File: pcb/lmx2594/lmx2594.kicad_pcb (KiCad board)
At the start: 4 copper layers, 48.3 x 48.3 mm, 87 parts, among them J1 Conn_Coaxial, J2 Conn_Coaxial, J3 Conn_01x13_Male, J4 Conn_Coaxial, J5 Conn_Coaxial, J6 Conn_Coaxial, J7 Conn_Coaxial, J8 Conn_Coaxial, J9 Conn_Coaxial, U1 L7812, U2 TPS62150, U3 lmx254

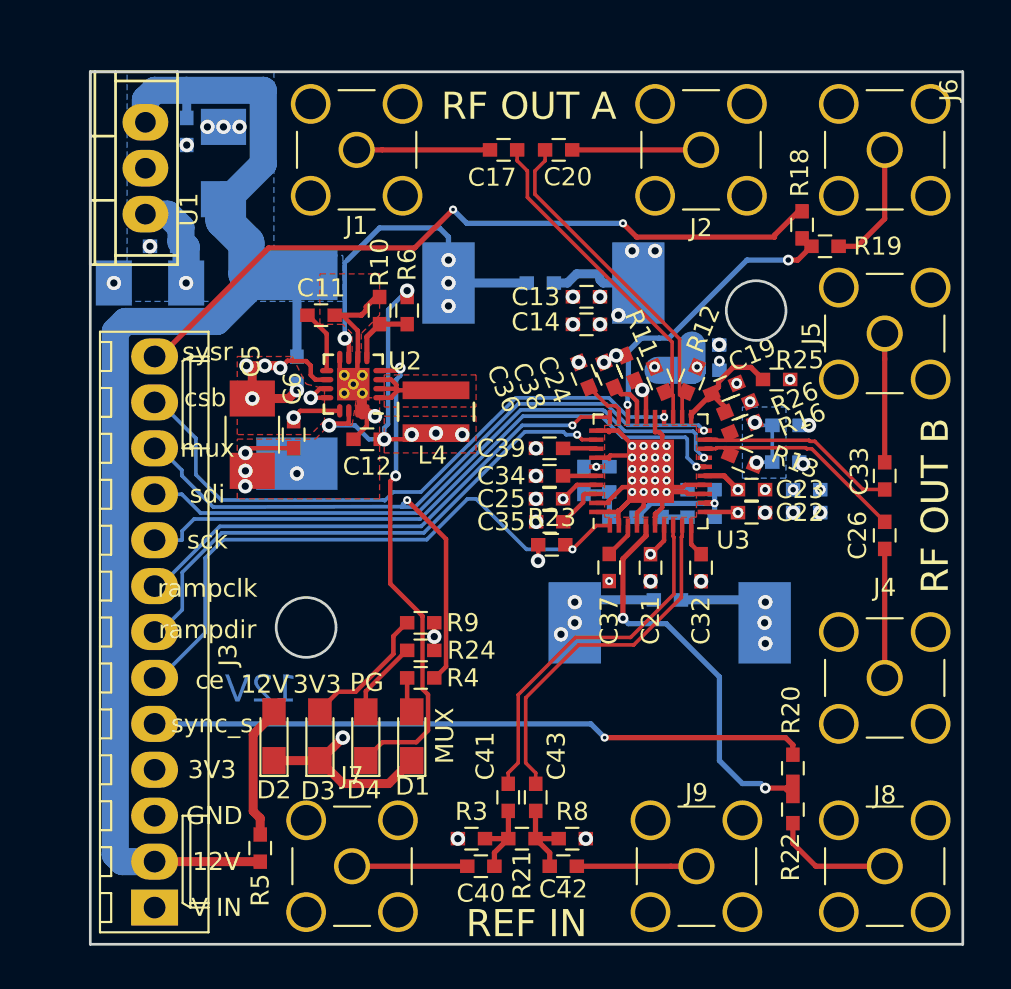
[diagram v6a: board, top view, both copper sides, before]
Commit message: additional fixes to silkscreen
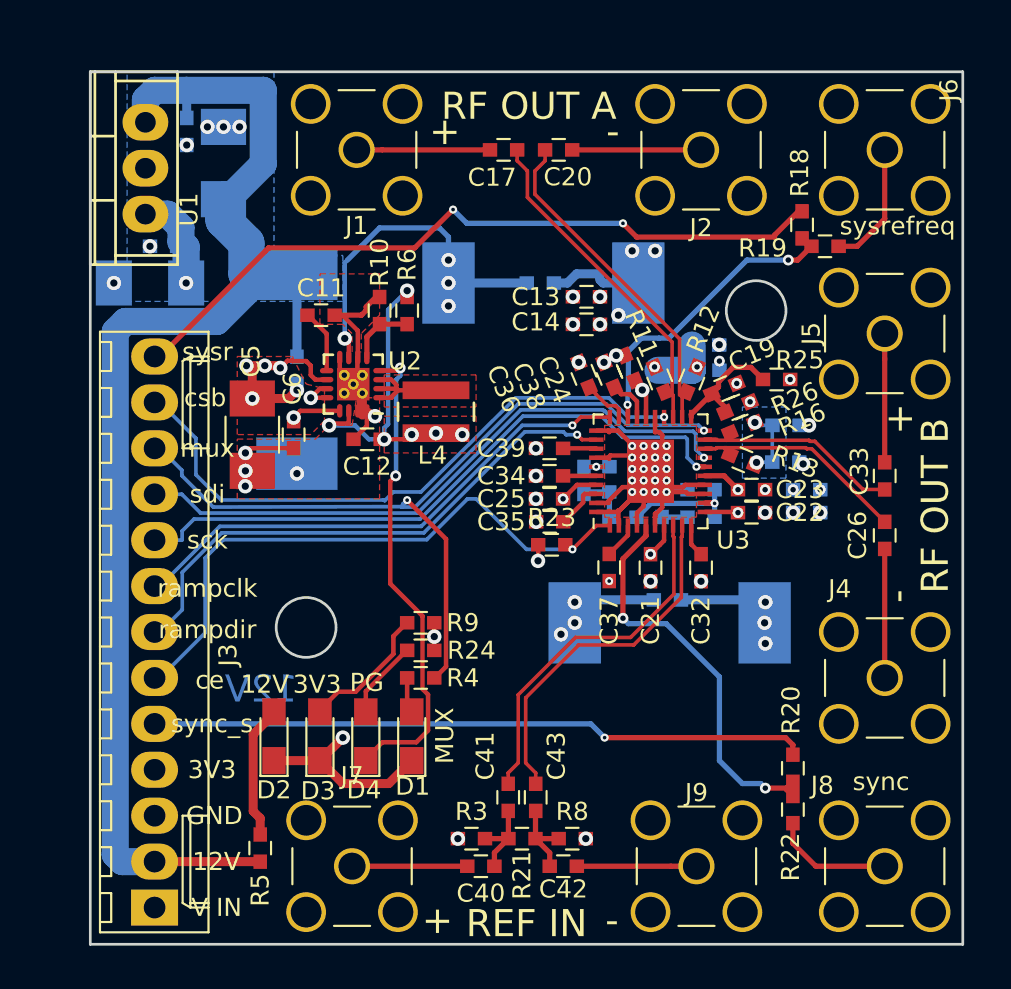
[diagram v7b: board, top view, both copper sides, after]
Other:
- board text added: "+"
- board text added: "-"
- board text added: "sync"
- board text added: "sysrefreq"
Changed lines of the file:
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@@
   (general
     (thickness 1.6)
-    (drawings 29)
+    (drawings 37)
     (tracks 902)
     (zones 0)
@@
   (page A4)
   (layers
-    (0 F.Cu signal)
+    (0 F.Cu signal hide)
     (1 In1.Cu signal hide)
     (2 In2.Cu signal hide)
@@
     (34 B.Paste user hide)
     (35 F.Paste user hide)
-    (36 B.SilkS user hide)
-    (37 F.SilkS user)
+    (36 B.SilkS user)
+    (37 F.SilkS user hide)
     (38 B.Mask user hide)
     (39 F.Mask user hide)
@@
     (descr "SMA pcb through hole jack")
     (tags "SMA THT Jack Straight")
-    (fp_text reference J4 (at 0 -5) (layer F.SilkS)
+    (fp_text reference J4 (at -2.4892 -4.9276) (layer F.SilkS)
       (effects (font (size 1 1) (thickness 0.15)))
     )
@@
     (descr "SMA pcb through hole jack")
     (tags "SMA THT Jack Straight")
-    (fp_text reference J8 (at 0 -3.937) (layer F.SilkS)
+    (fp_text reference J8 (at -3.4544 -4.4704) (layer F.SilkS)
       (effects (font (size 1 1) (thickness 0.15)))
     )
@@
     (tags "capacitor 0603")
     (attr smd)
-    (fp_text reference R19 (at 2.921 0) (layer F.SilkS)
+    (fp_text reference R19 (at -3.4544 0.1016) (layer F.SilkS)
       (effects (font (size 1 1) (thickness 0.15)))
     )
@@
     )
   )
+  (gr_text sync (at 117.3988 110.3884) (layer F.SilkS)
+    (effects (font (size 1 1) (thickness 0.25)))
+  )
+  (gr_text sysrefreq (at 118.3132 79.6544) (layer F.SilkS)
+    (effects (font (size 1 1) (thickness 0.25)))
+  )
+  (gr_text - (at 102.5652 74.422) (layer F.SilkS)
+    (effects (font (size 1.5 1.5) (thickness 0.3)))
+  )
+  (gr_text + (at 93.2688 74.422) (layer F.SilkS)
+    (effects (font (size 1.5 1.5) (thickness 0.3)))
+  )
+  (gr_text + (at 118.4656 90.2716) (layer F.SilkS)
+    (effects (font (size 1.5 1.5) (thickness 0.3)))
+  )
+  (gr_text - (at 118.3132 100.1268 90) (layer F.SilkS)
+    (effects (font (size 1.5 1.5) (thickness 0.3)))
+  )
+  (gr_text - (at 102.5144 118.0592) (layer F.SilkS)
+    (effects (font (size 1.5 1.5) (thickness 0.3)))
+  )
+  (gr_text + (at 92.8624 118.0592) (layer F.SilkS)
+    (effects (font (size 1.5 1.5) (thickness 0.3)))
+  )
   (gr_text MUX (at 93.2688 107.8484 90) (layer F.SilkS)

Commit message: Fixed diff pair impedance
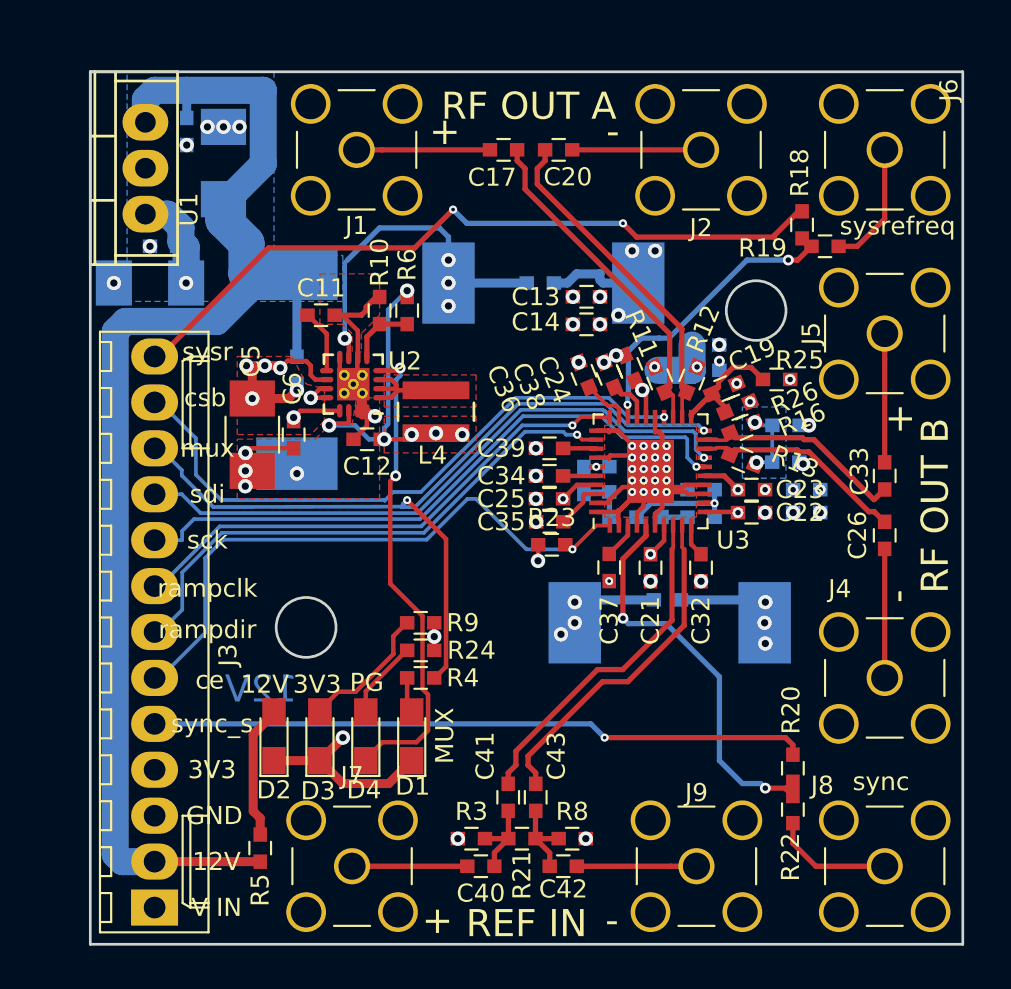
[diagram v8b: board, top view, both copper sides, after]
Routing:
- net /OSCIN_P: track 19.9 -> 18.9 mm
- net /OSCIN_N: track 19.9 -> 18.9 mm
